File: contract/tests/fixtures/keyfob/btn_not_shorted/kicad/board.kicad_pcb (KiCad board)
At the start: 2 copper layers, 36 x 22 mm, 8 parts, among them SW1 SW_Push, SW2 SW_Push, U1 EV1527

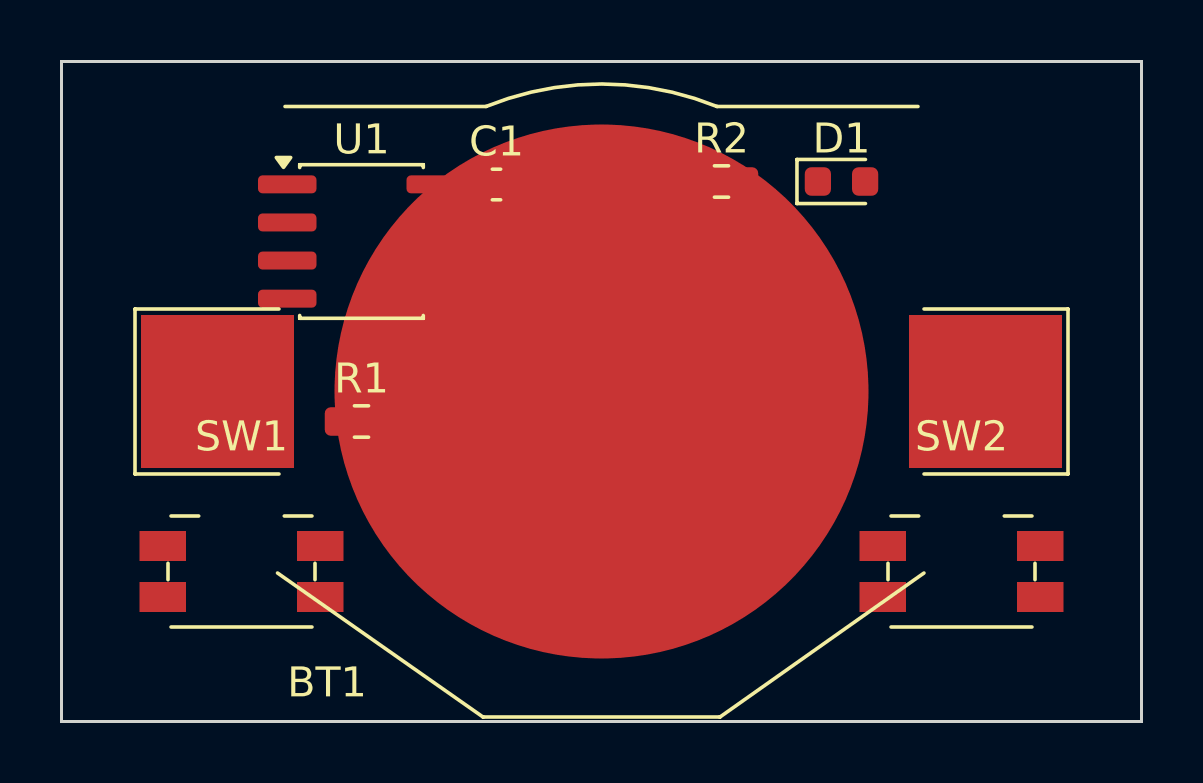
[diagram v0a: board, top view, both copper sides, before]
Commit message: test(contract): transmitter on the clean fob and five adversarial variants
The clean fixture gains U2, a SOT-23-6 stand-in transmitter on VCC/GND
with DATA on DOUT. Five <clause>--<case> variants each fail only their
named clause; all five were false passes under the previous grader.
_set_net keeps moving every pad of a repeated number.

Co-Authored-By: Claude Opus 5.5 <noreply@anthropic.com>
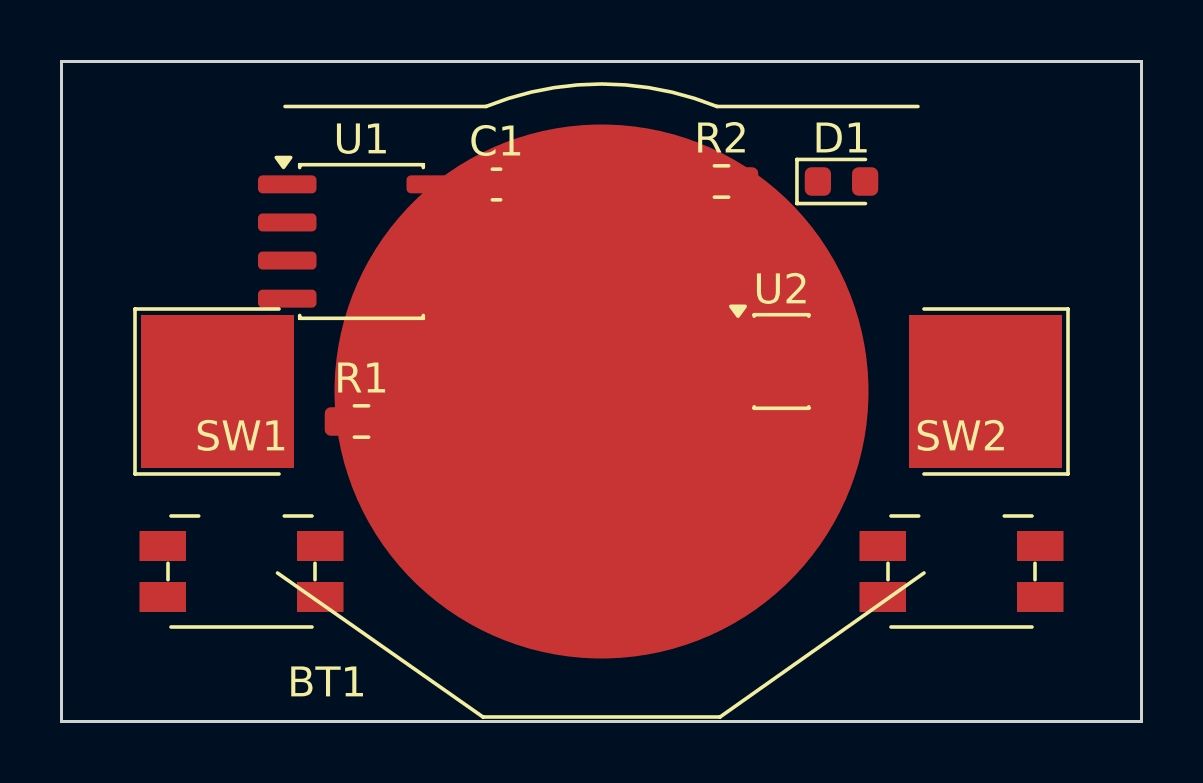
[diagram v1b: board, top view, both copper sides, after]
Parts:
- added U2: SYN115, Package_TO_SOT_SMD:SOT-23-6, F.Cu at (24.0, 10.0)
